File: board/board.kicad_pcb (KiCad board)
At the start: 2 copper layers, 21 x 13 mm, 1 part

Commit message: finished layout
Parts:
- added C1: 1uF, Capacitor_SMD:C_0603_1608Metric, F.Cu at (145.8, 101.5)
- added C2: 10uF, Capacitor_SMD:C_0603_1608Metric, F.Cu at (146.6, 99.1)
- added J1: 010_UART, on_edge:on_edge_2x05_host, F.Cu at (161.0, 96.5)
- added J2: 008_USB, on_edge:on_edge_2x05_device, F.Cu at (140.0, 96.5)
- added R1: 47.5k, Resistor_SMD:R_0603_1608Metric, F.Cu at (147.3, 101.5)
- added R2: 22.1k, Resistor_SMD:R_0603_1608Metric, F.Cu at (145.9, 96.8)
- added R3: 1k, Resistor_SMD:R_0603_1608Metric, F.Cu at (150.2, 101.5)
- added R4: 0R, Resistor_SMD:R_0603_1608Metric, F.Cu at (145.9, 93.8)
- added R6: 10k, Resistor_SMD:R_0603_1608Metric, F.Cu at (152.8, 101.5)
- added U1: CP2102N-Axx-xQFN28, Package_DFN_QFN:QFN-28-1EP_5x5mm_P0.5mm_EP3.35x3.35mm, F.Cu at (151.2, 96.6)
- LOGO1: moved to B.Cu
- moved LOGO1 3.06 mm to (151.4, 96.3), turned to 180 degrees
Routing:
- net GND: track 0.00 -> 56.0 mm, vias 0 -> 21
- net +5V: track 0.00 -> 26.9 mm, vias 0 -> 1
- net +3.3V: track 0.00 -> 19.5 mm, vias 0 -> 2
- net /cp2102/UART_RX: track 0.00 -> 9.93 mm
- net /cp2102/USRT_TX: track 0.00 -> 9.85 mm
- net Net-(U1-VBUS): track 0.00 -> 8.18 mm
- net /cp2102/USB_DM: track 0.00 -> 7.06 mm
- net /cp2102/USB_DP: track 0.00 -> 6.46 mm
- net /cp2102/USB_VBUS: track 0.00 -> 5.18 mm
- net Net-(U1-~{SUSPEND}): track 0.00 -> 2.39 mm
- net /cp2102/~{reset}: track 0.00 -> 1.62 mm
- added copper zone on B.Cu, net GND
- added copper zone on F.Cu, net GND
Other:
- outline, holes or cut-outs redrawn
- board text added: "osf.008"
- board text added: "osf.010"
- board text added: "osf.b139.v1.0"

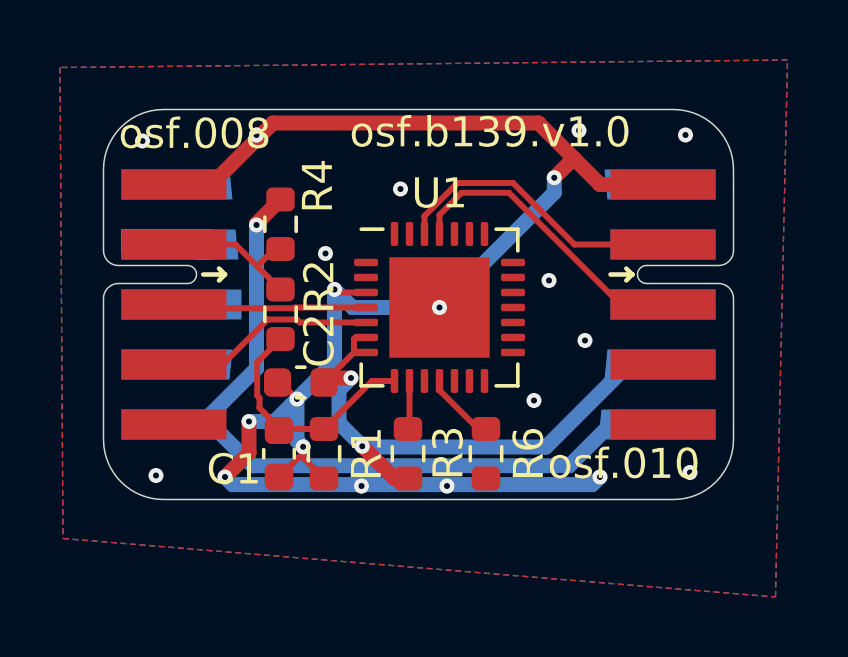
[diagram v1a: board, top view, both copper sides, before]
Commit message: added lcsc numbers
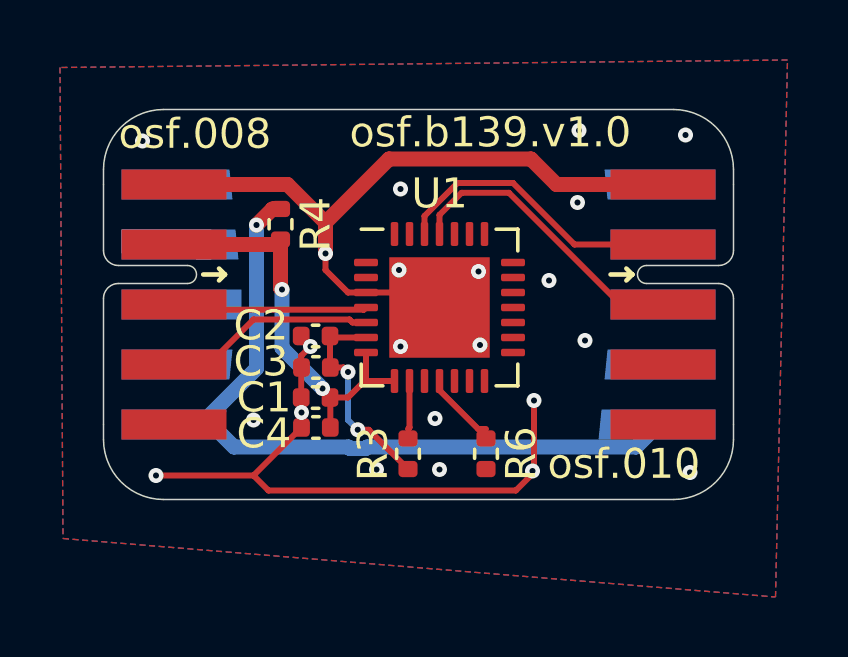
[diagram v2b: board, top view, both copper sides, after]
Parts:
- removed R1: 47.5k, Resistor_SMD:R_0603_1608Metric
- removed R2: 22.1k, Resistor_SMD:R_0603_1608Metric
- added C3: 1uF, Capacitor_SMD:C_0402_1005Metric, F.Cu at (147.1, 98.6)
- added C4: 1uF, Capacitor_SMD:C_0402_1005Metric, F.Cu at (147.1, 100.6)
- C1: value 1uF -> 100nF; footprint Capacitor_SMD:C_0603_1608Metric -> Capacitor_SMD:C_0402_1005Metric
- C2: value 10uF -> 100nF; footprint Capacitor_SMD:C_0603_1608Metric -> Capacitor_SMD:C_0402_1005Metric
- R3: value 1k -> 4.7k; footprint Resistor_SMD:R_0603_1608Metric -> Resistor_SMD:R_0402_1005Metric
- R4, R6: footprint Resistor_SMD:R_0603_1608Metric -> Resistor_SMD:R_0402_1005Metric
- moved C1 2.24 mm to (147.1, 99.6), turned to 180 degrees
- moved C2 1.63 mm to (147.1, 97.5)
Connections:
- C1 pad 1: Net-(U1-VBUS) -> /cp2102/USB_VBUS
- C2 pad 1: +3.3V -> Net-(U1-VDD)
- R3 pad 1: +3.3V -> Net-(U1-VDD)
- U1 pad 6: +3.3V -> Net-(U1-VDD)
- U1 pad 7: +3.3V -> /cp2102/USB_VBUS
- U1 pad 8: Net-(U1-VBUS) -> /cp2102/USB_VBUS
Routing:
- net +3.3V: track 19.5 -> 0.00 mm, vias 2 -> 0
- net GND: track 56.0 -> 45.0 mm, vias 21 -> 22
- net /cp2102/USB_VBUS: track 5.18 -> 13.5 mm, vias 0 -> 2
- net Net-(U1-VBUS): track 8.18 -> 0.00 mm
- net Net-(U1-VDD): track 0.00 -> 7.20 mm, vias 0 -> 2
- net +5V: track 26.9 -> 26.2 mm
